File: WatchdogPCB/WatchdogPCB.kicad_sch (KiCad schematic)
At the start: 38 parts, among them J1 Roll hoop, J2 Speed & Oil, J3 H bridge driver control, J4 Power, J5 Thermistor 1, J6 Thermistor 2, J7 Dashboard A, J8 Dashboard B, U1 A1301EUA-T, U2 MCP602, U3 DS3695N

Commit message: Board layout as contructed
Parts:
- C1, C2: footprint Capacitor_THT:C_Rect_L7.0mm_W2.5mm_P5.00mm -> Capacitor_THT:C_Rect_L10.0mm_W2.5mm_P7.50mm_MKS4
- D1: footprint Diode_THT:D_A-405_P10.16mm_Horizontal -> Diode_THT:D_A-405_P12.70mm_Horizontal
- R12, R9: footprint Resistor_THT:R_Axial_DIN0207_L6.3mm_D2.5mm_P7.62mm_Horizontal -> Resistor_THT:R_Axial_DIN0207_L6.3mm_D2.5mm_P10.16mm_Horizontal
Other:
- moved on the sheet: H1, H2, H3, H4
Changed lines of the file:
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@@
     )
   )
-  (symbol (lib_id "Mechanical:MountingHole") (at 256.54 92.71 0) (unit 1)
-    (in_bom yes) (on_board yes) (dnp no) (fields_autoplaced)
-    (property "Reference" "H2" (at 259.08 91.44 0)
-      (effects (font (size 1.27 1.27)) (justify left))
-    )
-    (property "Value" "MountingHole" (at 259.08 93.98 0)
-      (effects (font (size 1.27 1.27)) (justify left))
-    )
-    (property "Footprint" "MountingHole:MountingHole_3.2mm_M3_Pad" (at 256.54 92.71 0)
-      (effects (font (size 1.27 1.27)) hide)
-    )
-    (property "Datasheet" "~" (at 256.54 92.71 0)
+  (symbol (lib_id "Mechanical:MountingHole") (at 238.76 93.98 0) (unit 1)
+    (in_bom yes) (on_board yes) (dnp no) (fields_autoplaced)
+    (property "Reference" "H2" (at 241.3 92.71 0)
+      (effects (font (size 1.27 1.27)) (justify left))
+    )
+    (property "Value" "MountingHole" (at 241.3 95.25 0)
+      (effects (font (size 1.27 1.27)) (justify left))
+    )
+    (property "Footprint" "MountingHole:MountingHole_3.2mm_M3_Pad" (at 238.76 93.98 0)
+      (effects (font (size 1.27 1.27)) hide)
+    )
+    (property "Datasheet" "~" (at 238.76 93.98 0)
       (effects (font (size 1.27 1.27)) hide)
     )
@@
       (effects (font (size 1.27 1.27)))
     )
-    (property "Footprint" "Capacitor_THT:C_Rect_L7.0mm_W2.5mm_P5.00mm" (at 107.95 37.1348 0)
+    (property "Footprint" "Capacitor_THT:C_Rect_L10.0mm_W2.5mm_P7.50mm_MKS4" (at 107.95 37.1348 0)
       (effects (font (size 1.27 1.27)) hide)
     )
@@
       (effects (font (size 1.27 1.27)) (justify left))
     )
-    (property "Footprint" "Capacitor_THT:C_Rect_L7.0mm_W2.5mm_P5.00mm" (at 51.7652 175.26 0)
+    (property "Footprint" "Capacitor_THT:C_Rect_L10.0mm_W2.5mm_P7.50mm_MKS4" (at 51.7652 175.26 0)
       (effects (font (size 1.27 1.27)) hide)
     )
@@
       (effects (font (size 1.27 1.27)) (justify left))
     )
-    (property "Footprint" "Diode_THT:D_A-405_P10.16mm_Horizontal" (at 97.79 144.78 0)
+    (property "Footprint" "Diode_THT:D_A-405_P12.70mm_Horizontal" (at 97.79 144.78 0)
       (effects (font (size 1.27 1.27)) hide)
     )
@@
     )
   )
-  (symbol (lib_id "Mechanical:MountingHole") (at 256.54 97.79 0) (unit 1)
-    (in_bom yes) (on_board yes) (dnp no) (fields_autoplaced)
-    (property "Reference" "H3" (at 259.08 96.52 0)
-      (effects (font (size 1.27 1.27)) (justify left))
-    )
-    (property "Value" "MountingHole" (at 259.08 99.06 0)
-      (effects (font (size 1.27 1.27)) (justify left))
-    )
-    (property "Footprint" "MountingHole:MountingHole_3.2mm_M3_Pad" (at 256.54 97.79 0)
-      (effects (font (size 1.27 1.27)) hide)
-    )
-    (property "Datasheet" "~" (at 256.54 97.79 0)
+  (symbol (lib_id "Mechanical:MountingHole") (at 238.76 99.06 0) (unit 1)
+    (in_bom yes) (on_board yes) (dnp no) (fields_autoplaced)
+    (property "Reference" "H3" (at 241.3 97.79 0)
+      (effects (font (size 1.27 1.27)) (justify left))
+    )
+    (property "Value" "MountingHole" (at 241.3 100.33 0)
+      (effects (font (size 1.27 1.27)) (justify left))
+    )
+    (property "Footprint" "MountingHole:MountingHole_3.2mm_M3_Pad" (at 238.76 99.06 0)
+      (effects (font (size 1.27 1.27)) hide)
+    )
+    (property "Datasheet" "~" (at 238.76 99.06 0)
       (effects (font (size 1.27 1.27)) hide)
     )
@@
       (effects (font (size 1.27 1.27)) (justify left))
     )
-    (property "Footprint" "Resistor_THT:R_Axial_DIN0207_L6.3mm_D2.5mm_P7.62mm_Horizontal" (at 231.902 144.78 90)
+    (property "Footprint" "Resistor_THT:R_Axial_DIN0207_L6.3mm_D2.5mm_P10.16mm_Horizontal" (at 231.902 144.78 90)
       (effects (font (size 1.27 1.27)) hide)
     )
@@
       (effects (font (size 1.27 1.27)) (justify left))
     )
-    (property "Footprint" "Resistor_THT:R_Axial_DIN0207_L6.3mm_D2.5mm_P7.62mm_Horizontal" (at 229.362 26.67 90)
+    (property "Footprint" "Resistor_THT:R_Axial_DIN0207_L6.3mm_D2.5mm_P10.16mm_Horizontal" (at 229.362 26.67 90)
       (effects (font (size 1.27 1.27)) hide)
     )
@@
     )
   )
-  (symbol (lib_id "Mechanical:MountingHole") (at 256.54 87.63 0) (unit 1)
-    (in_bom yes) (on_board yes) (dnp no) (fields_autoplaced)
-    (property "Reference" "H1" (at 259.08 86.36 0)
-      (effects (font (size 1.27 1.27)) (justify left))
-    )
-    (property "Value" "MountingHole" (at 259.08 88.9 0)
-      (effects (font (size 1.27 1.27)) (justify left))
-    )
-    (property "Footprint" "MountingHole:MountingHole_3.2mm_M3_Pad" (at 256.54 87.63 0)
-      (effects (font (size 1.27 1.27)) hide)
-    )
-    (property "Datasheet" "~" (at 256.54 87.63 0)
+  (symbol (lib_id "Mechanical:MountingHole") (at 238.76 88.9 0) (unit 1)
+    (in_bom yes) (on_board yes) (dnp no) (fields_autoplaced)
+    (property "Reference" "H1" (at 241.3 87.63 0)
+      (effects (font (size 1.27 1.27)) (justify left))
+    )
+    (property "Value" "MountingHole" (at 241.3 90.17 0)
+      (effects (font (size 1.27 1.27)) (justify left))
+    )
+    (property "Footprint" "MountingHole:MountingHole_3.2mm_M3_Pad" (at 238.76 88.9 0)
+      (effects (font (size 1.27 1.27)) hide)
+    )
+    (property "Datasheet" "~" (at 238.76 88.9 0)
       (effects (font (size 1.27 1.27)) hide)
     )
@@
     )
   )
-  (symbol (lib_id "Mechanical:MountingHole") (at 256.54 102.87 0) (unit 1)
-    (in_bom yes) (on_board yes) (dnp no) (fields_autoplaced)
-    (property "Reference" "H4" (at 259.08 101.6 0)
-      (effects (font (size 1.27 1.27)) (justify left))
-    )
-    (property "Value" "MountingHole" (at 259.08 104.14 0)
-      (effects (font (size 1.27 1.27)) (justify left))
-    )
-    (property "Footprint" "MountingHole:MountingHole_3.2mm_M3_Pad" (at 256.54 102.87 0)
-      (effects (font (size 1.27 1.27)) hide)
-    )
-    (property "Datasheet" "~" (at 256.54 102.87 0)
-      (effects (font (size 1.27 1.27)) hide)
-    )
+  (symbol (lib_id "Mechanical:MountingHole") (at 238.76 104.14 0) (unit 1)
+    (in_bom yes) (on_board yes) (dnp no) (fields_autoplaced)
+    (property "Reference" "H4" (at 241.3 102.87 0)
+      (effects (font (size 1.27 1.27)) (justify left))
+    )
+    (property "Value" "MountingHole" (at 241.3 105.41 0)
+      (effects (font (size 1.27 1.27)) (justify left))
+    )
+    (property "Footprint" "MountingHole:MountingHole_3.2mm_M3_Pad" (at 238.76 104.14 0)
+      (effects (font (size 1.27 1.27)) hide)
+    )
+    (property "Datasheet" "~" (at 238.76 104.14 0)
+      (effects (font (size 1.27 1.27)) hide)
+    )

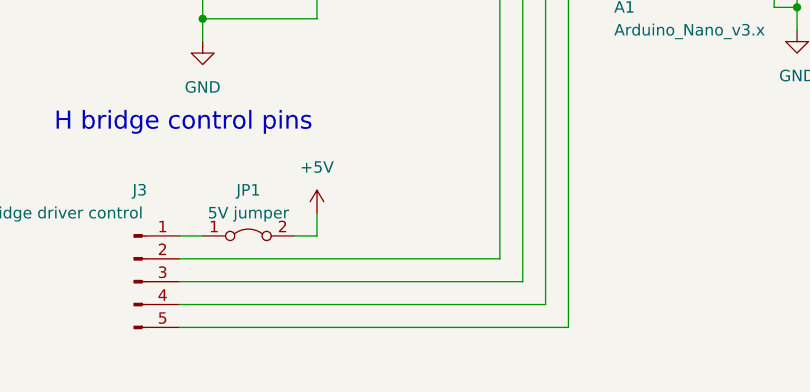
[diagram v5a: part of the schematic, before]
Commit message: Added button to UI
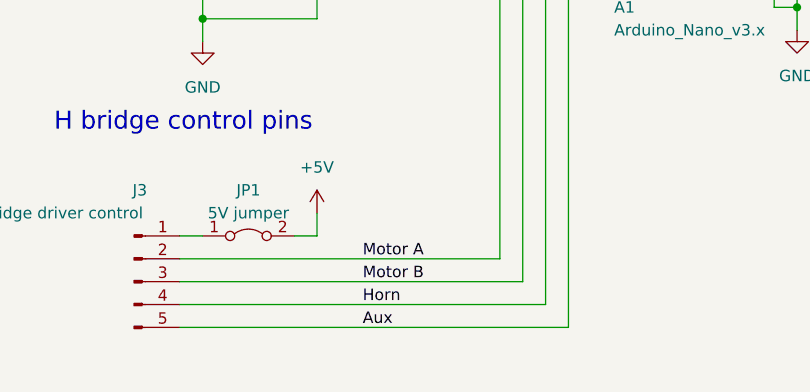
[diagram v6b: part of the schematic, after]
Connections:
- net Aux: now reaches A1.14 (D11), J3.5 (Pin_5)
- net Motor A: now reaches A1.6 (D3), J3.2 (Pin_2)
- net Motor B: now reaches A1.8 (D5), J3.3 (Pin_3)
- net Horn: now reaches A1.9 (D6), J3.4 (Pin_4)
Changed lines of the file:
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@@
+    (effects (font (size 1.27 1.27)) (justify left bottom))
+  )
+  (label "Aux" (at 102.87 185.42 0) (fields_autoplaced)
     (effects (font (size 1.27 1.27)) (justify left bottom))
   )
@@
   )
   (label "Hall effect" (at 50.8 99.06 0) (fields_autoplaced)
+    (effects (font (size 1.27 1.27)) (justify left bottom))
+  )
+  (label "Motor A" (at 102.87 177.8 0) (fields_autoplaced)
     (effects (font (size 1.27 1.27)) (justify left bottom))
   )
@@
     (effects (font (size 1.27 1.27)) (justify left bottom))
   )
+  (label "Horn" (at 102.87 182.88 0) (fields_autoplaced)
+    (effects (font (size 1.27 1.27)) (justify left bottom))
+  )
+  (label "Motor B" (at 102.87 180.34 0) (fields_autoplaced)
+    (effects (font (size 1.27 1.27)) (justify left bottom))
+  )

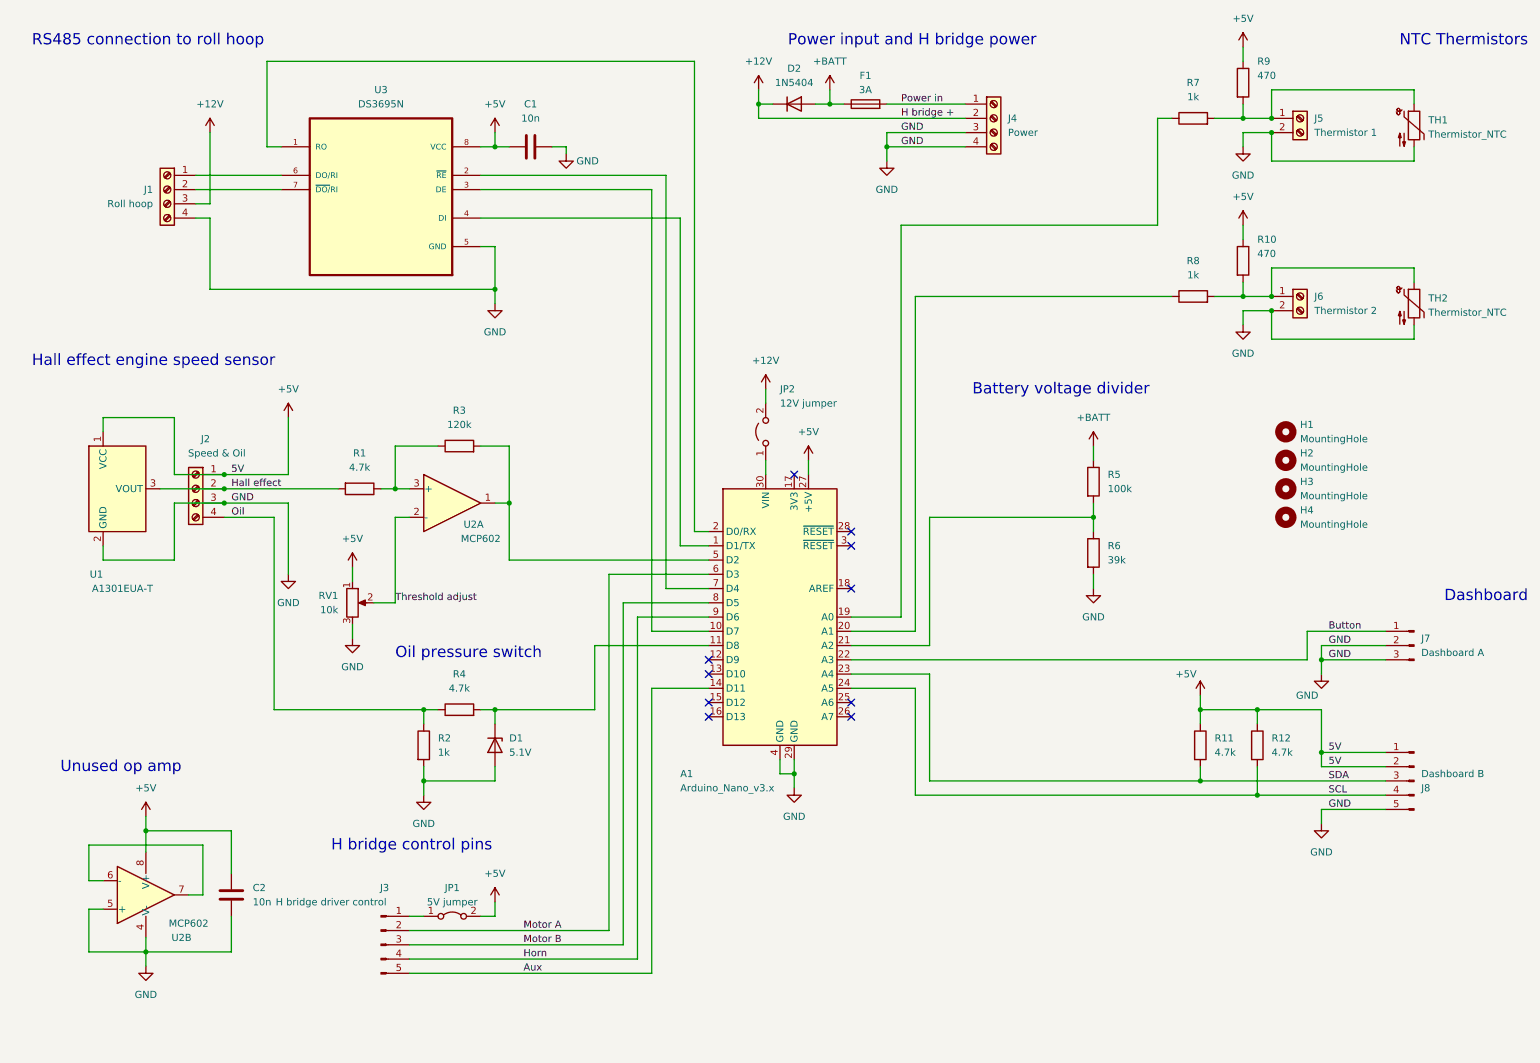
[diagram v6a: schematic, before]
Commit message: Schematics modified to use pages for wiring diagram, remote unit started, working on enclosure.
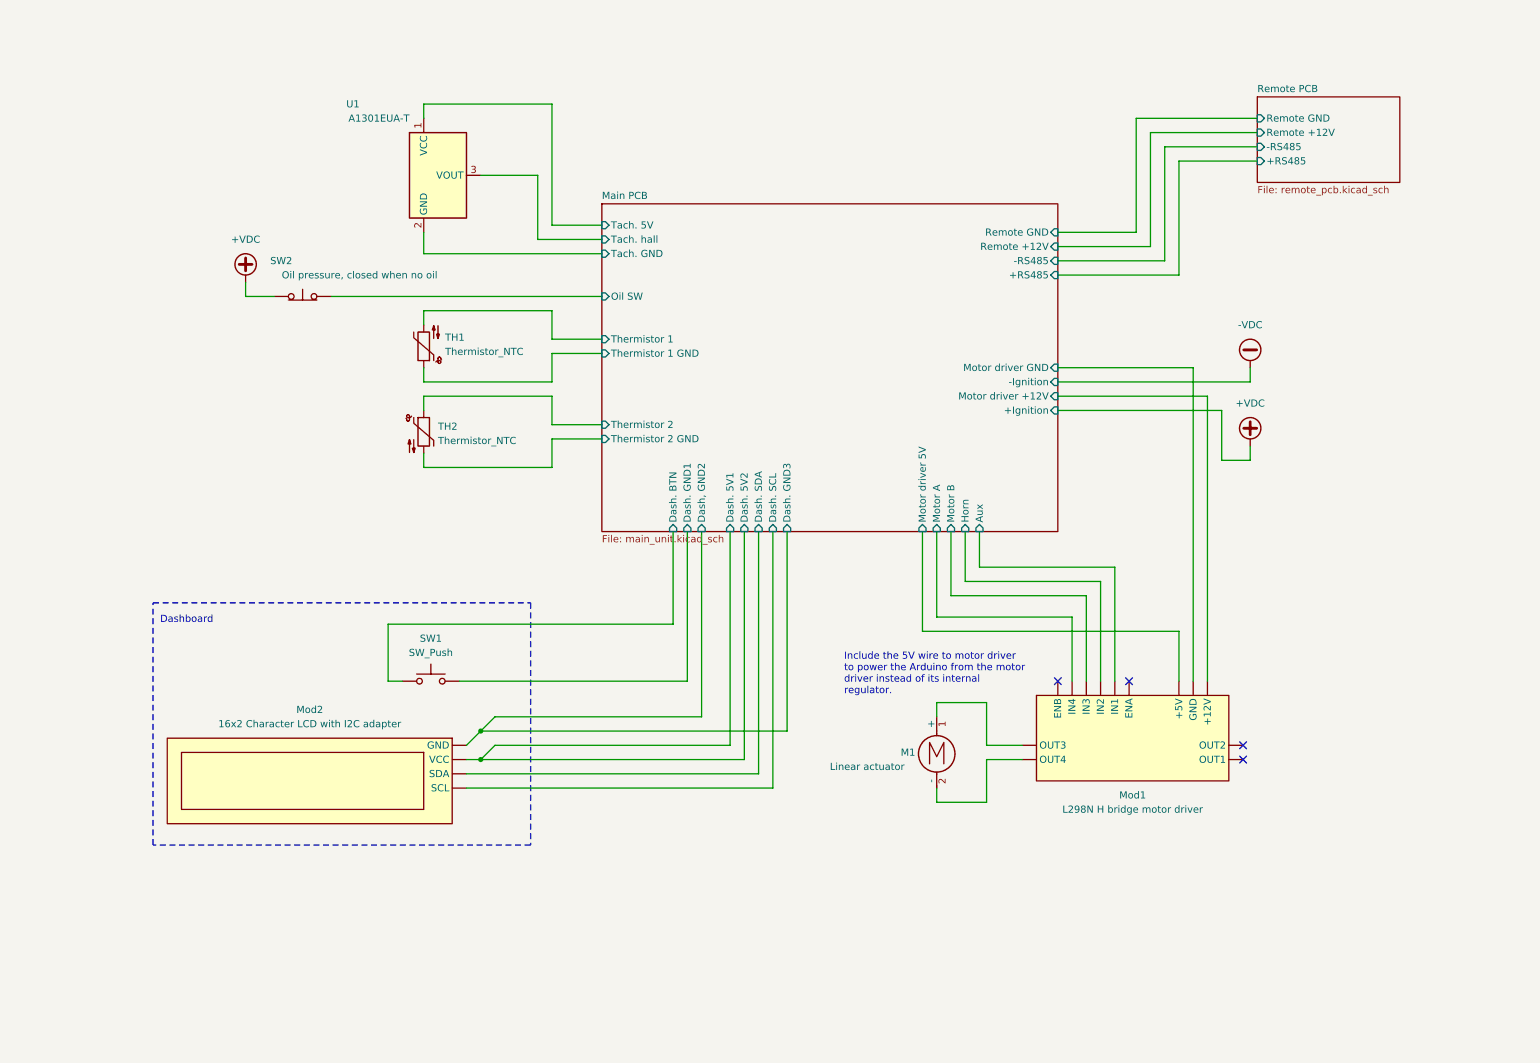
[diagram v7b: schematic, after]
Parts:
- removed A1: Arduino_Nano_v3.x, Module:Arduino_Nano, symbol MCU_Module:Arduino_Nano_v3.x
- removed C1, C2: 10n, Capacitor_THT:C_Rect_L10.0mm_W2.5mm_P7.50mm_MKS4, symbol Device:C
- removed D1: 5.1V, Diode_THT:D_A-405_P12.70mm_Horizontal, symbol Device:D_Zener
- removed D2: 1N5404, Diode_THT:D_DO-201AD_P15.24mm_Horizontal, symbol Diode:1N5404
- removed F1: 3A, Fuse:Fuse_Blade_ATO_directSolder, symbol Device:Fuse
- removed H1, H2, H3, H4: MountingHole, MountingHole:MountingHole_3.2mm_M3_Pad, symbol Mechanical:MountingHole
- removed J1: Roll hoop, TerminalBlock:TerminalBlock_bornier-4_P5.08mm, symbol Connector:Screw_Terminal_01x04
- removed J2: Speed & Oil, TerminalBlock:TerminalBlock_bornier-4_P5.08mm, symbol Connector:Screw_Terminal_01x04
- removed J3: H bridge driver control, Connector_PinHeader_2.54mm:PinHeader_1x05_P2.54mm_Vertical, symbol Connector:Conn_01x05_Pin
- removed J4: Power, TerminalBlock:TerminalBlock_bornier-4_P5.08mm, symbol Connector:Screw_Terminal_01x04
- removed J5: Thermistor 1, TerminalBlock:TerminalBlock_bornier-2_P5.08mm, symbol Connector:Screw_Terminal_01x02
- removed J6: Thermistor 2, TerminalBlock:TerminalBlock_bornier-2_P5.08mm, symbol Connector:Screw_Terminal_01x02
- removed J7: Dashboard A, Connector_JST:JST_XH_B3B-XH-A_1x03_P2.50mm_Vertical, symbol Connector:Conn_01x03_Pin
- removed J8: Dashboard B, Connector_JST:JST_XH_B5B-XH-A_1x05_P2.50mm_Vertical, symbol Connector:Conn_01x05_Pin
- removed JP1: 5V jumper, Connector_PinSocket_2.54mm:PinSocket_1x02_P2.54mm_Vertical, symbol Jumper:Jumper_2_Bridged
- removed JP2: 12V jumper, Connector_PinSocket_2.54mm:PinSocket_1x02_P2.54mm_Vertical, symbol Jumper:Jumper_2_Open
- removed R1, R11, R4: 4.7k, Resistor_THT:R_Axial_DIN0207_L6.3mm_D2.5mm_P7.62mm_Horizontal, symbol Device:R
- removed R10: 470, Resistor_THT:R_Axial_DIN0207_L6.3mm_D2.5mm_P7.62mm_Horizontal, symbol Device:R
- removed R12: 4.7k, Resistor_THT:R_Axial_DIN0207_L6.3mm_D2.5mm_P10.16mm_Horizontal, symbol Device:R
- removed R2, R7, R8: 1k, Resistor_THT:R_Axial_DIN0207_L6.3mm_D2.5mm_P7.62mm_Horizontal, symbol Device:R
- removed R3: 120k, Resistor_THT:R_Axial_DIN0207_L6.3mm_D2.5mm_P7.62mm_Horizontal, symbol Device:R
- removed R5: 100k, Resistor_THT:R_Axial_DIN0207_L6.3mm_D2.5mm_P7.62mm_Horizontal, symbol Device:R
- removed R6: 39k, Resistor_THT:R_Axial_DIN0207_L6.3mm_D2.5mm_P7.62mm_Horizontal, symbol Device:R
- removed R9: 470, Resistor_THT:R_Axial_DIN0207_L6.3mm_D2.5mm_P10.16mm_Horizontal, symbol Device:R
- removed RV1: 10k, Potentiometer_THT:Potentiometer_Piher_PT-10-V10_Vertical_Hole, symbol Device:R_Potentiometer
- removed U2: MCP602, Package_DIP:DIP-8_W7.62mm_Socket_LongPads, symbol Amplifier_Operational:MCP602
- removed U3: DS3695N, Package_DIP:DIP-8_W7.62mm_Socket_LongPads, symbol DS3695N:DS3695N
- added M1: Linear actuator, symbol Motor:Motor_DC
- added Mod1: L298N H bridge motor driver, symbol Custom:L298N_Motor_Driver_H_Bridge
- added Mod2: 16x2 Character LCD with I2C adapter, symbol Custom:16x2_Character_LCD_with_I2C_adapter
- added SW1: SW_Push, symbol Switch:SW_Push
- added SW2: Oil pressure, closed when no oil, symbol Switch:SW_Push_Open
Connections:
- net Main PCB/Thermistor 2: now reaches TH2.1
- net Main PCB/Thermistor 1 GND: now reaches TH1.1
- net +5V renamed Main PCB/Tach. 5V
- removed net GND: TH1.2, TH2.2, U1.2 (GND)
- net Hall effect renamed Main PCB/Tach. hall
- new net: M1.1 (+), Mod1. (OUT4)
- new net: M1.2 (-), Mod1. (OUT4)
- new net +VDC: SW2.1 (A)
- new net Main PCB/Aux: Mod1. (OUT4)
- new net Main PCB/Dash, GND2: Mod2. (VCC)
- new net Main PCB/Dash. 5V1: Mod2. (VCC)
- new net Main PCB/Dash. BTN: SW1.1
- new net Main PCB/Dash. GND1: SW1.2
- new net Main PCB/Dash. SCL: Mod2. (VCC)
- new net Main PCB/Dash. SDA: Mod2. (VCC)
- new net Main PCB/Horn: Mod1. (OUT4)
- new net Main PCB/Motor A: Mod1. (OUT4)
- new net Main PCB/Motor B: Mod1. (OUT4)
- new net Main PCB/Motor driver +12V: Mod1. (OUT4)
- new net Main PCB/Motor driver 5V: Mod1. (OUT4)
- new net Main PCB/Motor driver GND: Mod1. (OUT4)
- new net Main PCB/Oil SW: SW2.2 (B)
- new net Main PCB/Tach. GND: U1.2 (GND)
- new net Main PCB/Thermistor 1: TH1.2
- new net Main PCB/Thermistor 2 GND: TH2.2
- no-connect marks 10 -> 4
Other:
- added sheet Main PCB (main_unit.kicad_sch)
- added sheet Remote PCB (remote_pcb.kicad_sch)
- note added: "Include the 5V wire to motor driver to power the Arduino from the motor driver instead of its internal regulator."
- note removed: "Battery voltage divider"
- note removed: "H bridge control pins"
- note removed: "Hall effect engine speed sensor"
- note removed: "NTC Thermistors"
- note removed: "Oil pressure switch"
- note removed: "Power input and H bridge power"
- note removed: "RS485 connection to roll hoop"
- note removed: "Unused op amp"
- title: Tractor Engine Watchdog ->  Tractor Engine Watchdog - Wiring diagram
